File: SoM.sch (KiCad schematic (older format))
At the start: 6 parts, among them U8 SA800U-WF

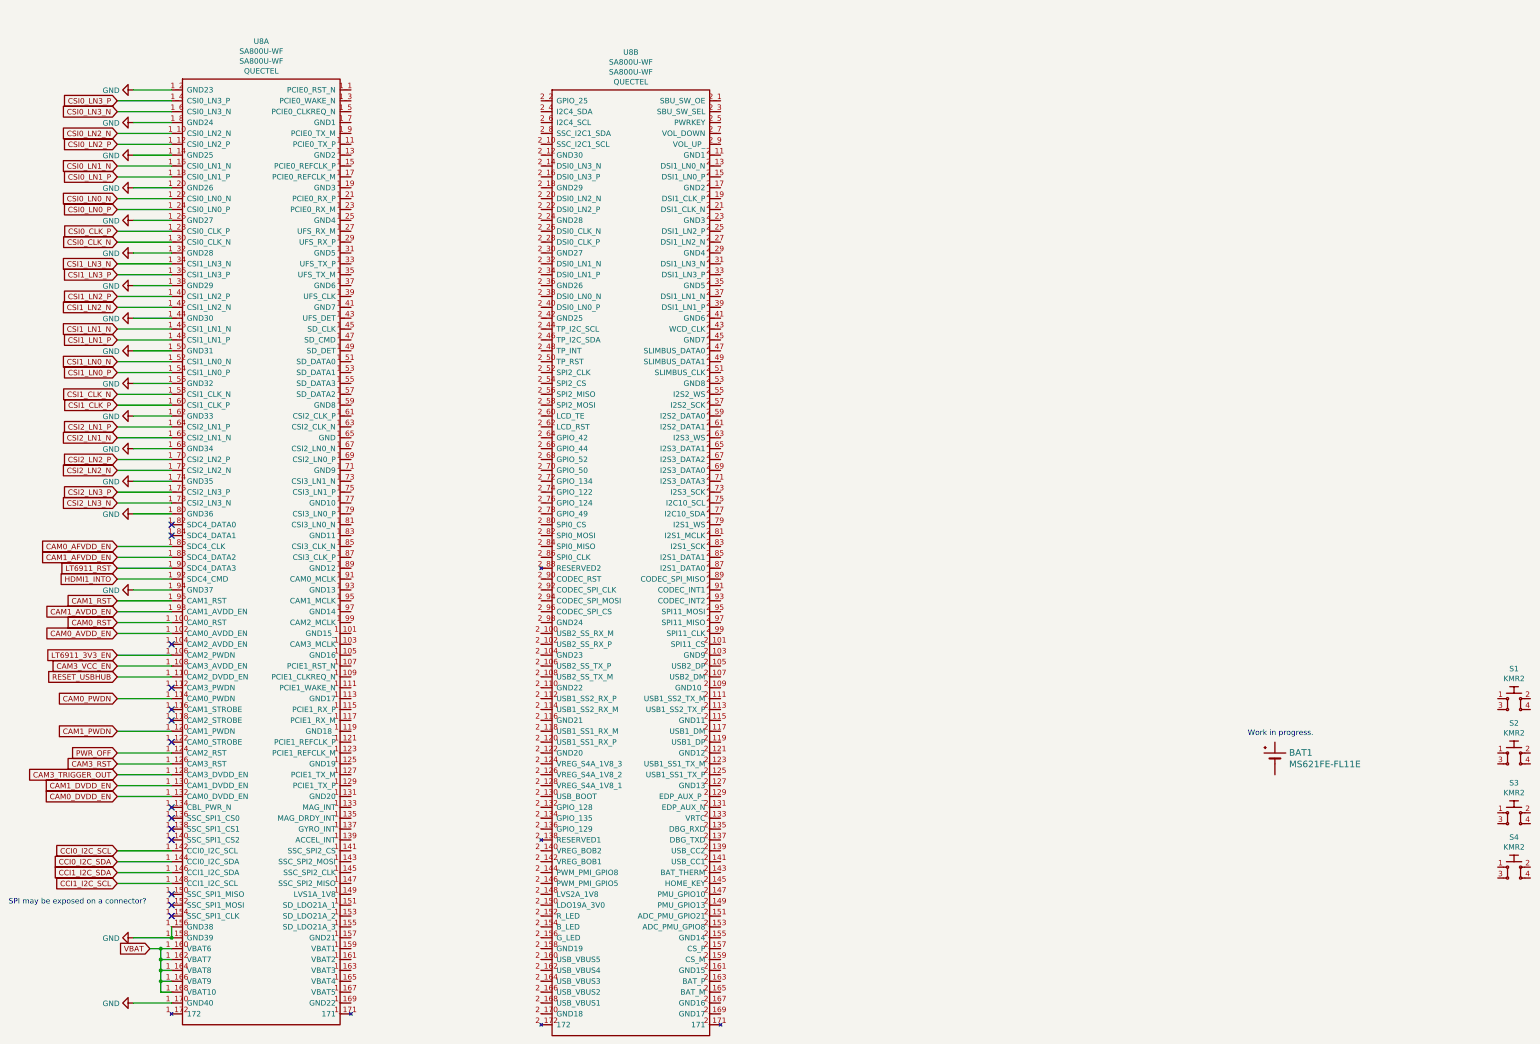
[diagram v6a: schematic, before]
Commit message: added an initial version of SoM
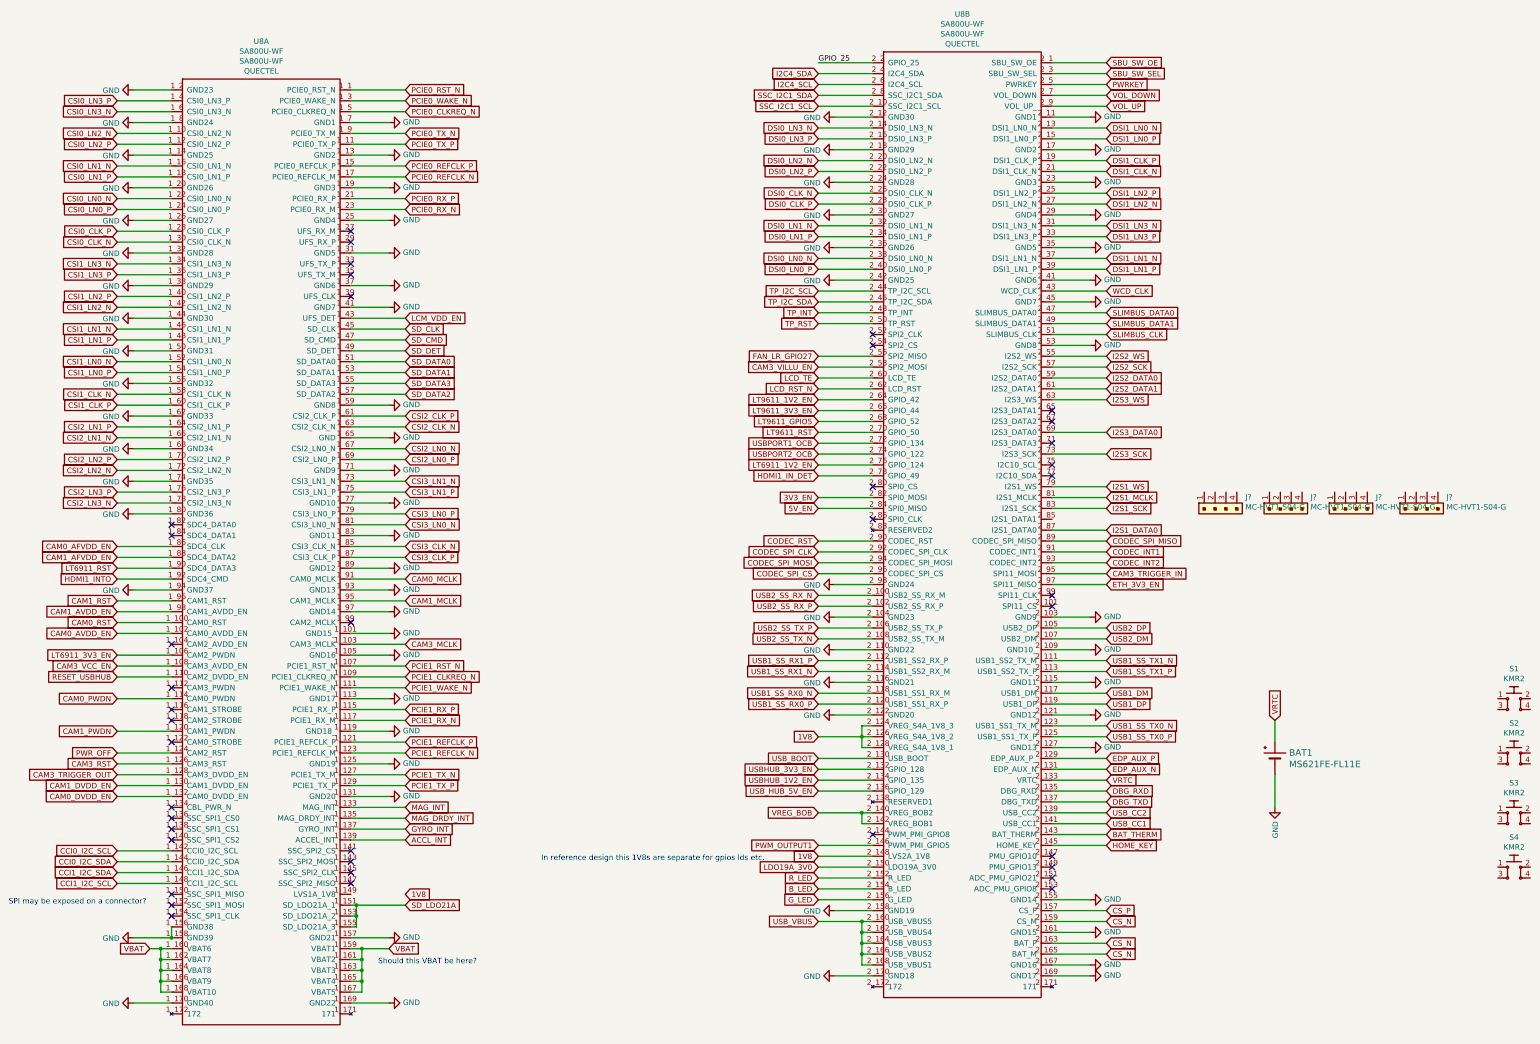
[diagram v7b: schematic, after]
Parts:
- added J? (x4): MC-HVT1-S04-G, antmicro-footprints:PinHeader_1x4_P1.27mm_Drill.7mm, symbol antmicroRectangularConnectorsHeadersMalePins:MC-HVT1-S04-G
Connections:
- net GND: now also BAT1.-, U8.1_101 (GND15_), U8.1_105 (GND16), U8.1_113 (GND17), U8.1_119 (GND18_), U8.1_125 (GND19), U8.1_13 (GND2), U8.1_131 (GND20), U8.1_157 (GND21), U8.1_169 (GND22), U8.1_19 (GND3), U8.1_25 (GND4), U8.1_31 (GND5), U8.1_37 (GND6), U8.1_41 (GND7), U8.1_59 (GND8), U8.1_65 (GND), U8.1_7 (GND1), U8.1_71 (GND9), U8.1_77 (GND10), U8.1_83 (GND11), U8.1_89 (GND12), U8.1_93 (GND13), U8.1_97 (GND14), U8.2_103 (GND9), U8.2_104 (GND23), U8.2_109 (GND10_), U8.2_11 (GND1), U8.2_110 (GND22), U8.2_115 (GND11), U8.2_116 (GND21), U8.2_12 (GND30), U8.2_121 (GND12), U8.2_122 (GND20), U8.2_127 (GND13), U8.2_155 (GND14), U8.2_158 (GND19), U8.2_161 (GND15), U8.2_167 (GND16), U8.2_169 (GND17), U8.2_17 (GND2), U8.2_170 (GND18), U8.2_18 (GND29), U8.2_23 (GND3), U8.2_24 (GND28), U8.2_29 (GND4), U8.2_30 (GND27), U8.2_35 (GND5), U8.2_36 (GND26), U8.2_41 (GND6), U8.2_42 (GND25), U8.2_45 (GND7), U8.2_53 (GND8), U8.2_98 (GND24)
- net VBAT: now also U8.1_159 (VBAT1), U8.1_161 (VBAT2), U8.1_163 (VBAT3), U8.1_165 (VBAT4), U8.1_167 (VBAT5)
- net VRTC: now reaches BAT1.+
- net VRTC: now also U8.2_133 (VRTC)
- net PCIE0_RST_N: now reaches U8.1_1 (PCIE0_RST_N)
- net CAM3_MCLK: now reaches U8.1_103 (CAM3_MCLK)
- net PCIE1_RST_N: now reaches U8.1_107 (PCIE1_RST_N)
- net PCIE1_CLKREQ_N: now reaches U8.1_109 (PCIE1_CLKREQ_N)
- net PCIE0_TX_P: now reaches U8.1_11 (PCIE0_TX_P)
- net PCIE1_WAKE_N: now reaches U8.1_111 (PCIE1_WAKE_N)
- net PCIE1_RX_P: now reaches U8.1_115 (PCIE1_RX_P)
- net PCIE1_RX_N: now reaches U8.1_117 (PCIE1_RX_M)
- net PCIE1_REFCLK_P: now reaches U8.1_121 (PCIE1_REFCLK_P)
- net PCIE1_REFCLK_N: now reaches U8.1_123 (PCIE1_REFCLK_M)
- net PCIE1_TX_N: now reaches U8.1_127 (PCIE1_TX_M)
- net PCIE1_TX_P: now reaches U8.1_129 (PCIE1_TX_P)
- net MAG_INT: now reaches U8.1_133 (MAG_INT)
- net MAG_DRDY_INT: now reaches U8.1_135 (MAG_DRDY_INT)
- net GYRO_INT: now reaches U8.1_137 (GYRO_INT)
- net ACCL_INT: now reaches U8.1_139 (ACCEL_INT)
- net PCIE0_REFCLK_P: now reaches U8.1_15 (PCIE0_REFCLK_P)
- net SD_LDO21A: now reaches U8.1_151 (SD_LDO21A_1)
- net SD_LDO21A: now also U8.1_153 (SD_LDO21A_2), U8.1_155 (SD_LDO21A_3)
- net PCIE0_REFCLK_N: now reaches U8.1_17 (PCIE0_REFCLK_M)
- net PCIE0_RX_P: now reaches U8.1_21 (PCIE0_RX_P)
- net PCIE0_RX_N: now reaches U8.1_23 (PCIE0_RX_M)
- net PCIE0_WAKE_N: now reaches U8.1_3 (PCIE0_WAKE_N)
- net LCM_VDD_EN: now reaches U8.1_43 (UFS_DET)
- net SD_CLK: now reaches U8.1_45 (SD_CLK)
- net SD_CMD: now reaches U8.1_47 (SD_CMD)
- net SD_DET: now reaches U8.1_49 (SD_DET)
- net PCIE0_CLKREQ_N: now reaches U8.1_5 (PCIE0_CLKREQ_N)
- net SD_DATA0: now reaches U8.1_51 (SD_DATA0)
- net SD_DATA1: now reaches U8.1_53 (SD_DATA1)
- net SD_DATA3: now reaches U8.1_55 (SD_DATA3)
- net SD_DATA2: now reaches U8.1_57 (SD_DATA2)
- net CSI2_CLK_P: now reaches U8.1_61 (CSI2_CLK_P)
- net CSI2_CLK_N: now reaches U8.1_63 (CSI2_CLK_N)
- net CSI2_LN0_N: now reaches U8.1_67 (CSI2_LN0_N)
- net CSI2_LN0_P: now reaches U8.1_69 (CSI2_LN0_P)
- net CSI3_LN1_N: now reaches U8.1_73 (CSI3_LN1_N)
- net CSI3_LN1_P: now reaches U8.1_75 (CSI3_LN1_P)
- net CSI3_LN0_P: now reaches U8.1_79 (CSI3_LN0_P)
- net CSI3_LN0_N: now reaches U8.1_81 (CSI3_LN0_N)
- net CSI3_CLK_N: now reaches U8.1_85 (CSI3_CLK_N)
- net CSI3_CLK_P: now reaches U8.1_87 (CSI3_CLK_P)
- net PCIE0_TX_N: now reaches U8.1_9 (PCIE0_TX_M)
- net CAM0_MCLK: now reaches U8.1_91 (CAM0_MCLK)
- net CAM1_MCLK: now reaches U8.1_95 (CAM1_MCLK)
- net SBU_SW_OE: now reaches U8.2_1 (SBU_SW_OE)
- net SSC_I2C1_SCL: now reaches U8.2_10 (SSC_I2C1_SCL)
- net USB2_SS_RX_N: now reaches U8.2_100 (USB2_SS_RX_M)
- net USB2_SS_RX_P: now reaches U8.2_102 (USB2_SS_RX_P)
- net USB2_DP: now reaches U8.2_105 (USB2_DP)
- net USB2_SS_TX_P: now reaches U8.2_106 (USB2_SS_TX_P)
- net USB2_DM: now reaches U8.2_107 (USB2_DM)
- net USB2_SS_TX_N: now reaches U8.2_108 (USB2_SS_TX_M)
- net USB1_SS_TX1_N: now reaches U8.2_111 (USB1_SS2_TX_M)
- net USB1_SS_RX1_P: now reaches U8.2_112 (USB1_SS2_RX_P)
- net USB1_SS_TX1_P: now reaches U8.2_113 (USB1_SS2_TX_P)
- net USB1_SS_RX1_N: now reaches U8.2_114 (USB1_SS2_RX_M)
- net USB1_DM: now reaches U8.2_117 (USB1_DM)
- net USB1_SS_RX0_N: now reaches U8.2_118 (USB1_SS1_RX_M)
- net USB1_DP: now reaches U8.2_119 (USB1_DP)
- net USB1_SS_RX0_P: now reaches U8.2_120 (USB1_SS1_RX_P)
- net USB1_SS_TX0_N: now reaches U8.2_123 (USB1_SS1_TX_M)
- net 1V8: now reaches U8.2_124 (VREG_S4A_1V8_3)
- net 1V8: now also U8.2_126 (VREG_S4A_1V8_2), U8.2_128 (VREG_S4A_1V8_1), U8.2_148 (LVS2A_1V8)
- net USB1_SS_TX0_P: now reaches U8.2_125 (USB1_SS1_TX_P)
- net EDP_AUX_P: now reaches U8.2_129 (EDP_AUX_P_)
- net DSI1_LN0_N: now reaches U8.2_13 (DSI1_LN0_N)
- net USB_BOOT: now reaches U8.2_130 (USB_BOOT)
- net EDP_AUX_N: now reaches U8.2_131 (EDP_AUX_N)
- net USBHUB_3V3_EN: now reaches U8.2_132 (GPIO_128)
- net USBHUB_1V2_EN: now reaches U8.2_134 (GPIO_135)
- net DBG_RXD: now reaches U8.2_135 (DBG_RXD)
- net USB_HUB_5V_EN: now reaches U8.2_136 (GPIO_129)
- net DBG_TXD: now reaches U8.2_137 (DBG_TXD)
- net USB_CC2: now reaches U8.2_139 (USB_CC2)
- net DSI0_LN3_N: now reaches U8.2_14 (DSI0_LN3_N)
- net VREG_BOB: now reaches U8.2_140 (VREG_BOB2)
- net VREG_BOB: now also U8.2_142 (VREG_BOB1)
- net USB_CC1: now reaches U8.2_141 (USB_CC1)
- net BAT_THERM: now reaches U8.2_143 (BAT_THERM)
- net HOME_KEY: now reaches U8.2_145 (HOME_KEY)
- net PWM_OUTPUT1: now reaches U8.2_146 (PWM_PMI_GPIO5)
- net DSI1_LN0_P: now reaches U8.2_15 (DSI1_LN0_P)
- net LDO19A_3V0: now reaches U8.2_150 (LDO19A_3V0)
- net R_LED: now reaches U8.2_152 (R_LED)
- net B_LED: now reaches U8.2_154 (B_LED)
- net G_LED: now reaches U8.2_156 (G_LED)
- net CS_P: now reaches U8.2_157 (CS_P)
- net CS_N: now reaches U8.2_159 (CS_M)
- net CS_N: now also U8.2_163 (BAT_P), U8.2_165 (BAT_M)
- net DSI0_LN3_P: now reaches U8.2_16 (DSI0_LN3_P)
- net USB_VBUS: now reaches U8.2_160 (USB_VBUS5)
- net USB_VBUS: now also U8.2_162 (USB_VBUS4), U8.2_164 (USB_VBUS3), U8.2_166 (USB_VBUS2), U8.2_168 (USB_VBUS1)
- net DSI1_CLK_P: now reaches U8.2_19 (DSI1_CLK_P)
- net GPIO_25: now reaches U8.2_2 (GPIO_25)
- net DSI0_LN2_N: now reaches U8.2_20 (DSI0_LN2_N)
- net DSI1_CLK_N: now reaches U8.2_21 (DSI1_CLK_N)
- net DSI0_LN2_P: now reaches U8.2_22 (DSI0_LN2_P)
- net DSI1_LN2_P: now reaches U8.2_25 (DSI1_LN2_P)
- net DSI0_CLK_N: now reaches U8.2_26 (DSI0_CLK_N)
- net DSI1_LN2_N: now reaches U8.2_27 (DSI1_LN2_N)
- net DSI0_CLK_P: now reaches U8.2_28 (DSI0_CLK_P)
- net SBU_SW_SEL: now reaches U8.2_3 (SBU_SW_SEL)
- net DSI1_LN3_N: now reaches U8.2_31 (DSI1_LN3_N)
- net DSI0_LN1_N: now reaches U8.2_32 (DSI0_LN1_N)
- net DSI1_LN3_P: now reaches U8.2_33 (DSI1_LN3_P)
- net DSI0_LN1_P: now reaches U8.2_34 (DSI0_LN1_P)
- net DSI1_LN1_N: now reaches U8.2_37 (DSI1_LN1_N)
- net DSI0_LN0_N: now reaches U8.2_38 (DSI0_LN0_N)
- net DSI1_LN1_P: now reaches U8.2_39 (DSI1_LN1_P)
- net I2C4_SDA: now reaches U8.2_4 (I2C4_SDA)
- net DSI0_LN0_P: now reaches U8.2_40 (DSI0_LN0_P)
- net WCD_CLK: now reaches U8.2_43 (WCD_CLK)
- net TP_I2C_SCL: now reaches U8.2_44 (TP_I2C_SCL)
- net TP_I2C_SDA: now reaches U8.2_46 (TP_I2C_SDA)
- net SLIMBUS_DATA0: now reaches U8.2_47 (SLIMBUS_DATA0)
- net TP_INT: now reaches U8.2_48 (TP_INT)
- net SLIMBUS_DATA1: now reaches U8.2_49 (SLIMBUS_DATA1)
- net PWRKEY: now reaches U8.2_5 (PWRKEY)
- net TP_RST: now reaches U8.2_50 (TP_RST)
- net SLIMBUS_CLK: now reaches U8.2_51 (SLIMBUS_CLK)
- net I2S2_WS: now reaches U8.2_55 (I2S2_WS)
- net FAN_LR_GPIO27: now reaches U8.2_56 (SPI2_MISO)
- net I2S2_SCK: now reaches U8.2_57 (I2S2_SCK)
- net CAM3_VILLU_EN: now reaches U8.2_58 (SPI2_MOSI)
- net I2S2_DATA0: now reaches U8.2_59 (I2S2_DATA0)
- net I2C4_SCL: now reaches U8.2_6 (I2C4_SCL)
- net LCD_TE: now reaches U8.2_60 (LCD_TE)
- net I2S2_DATA1: now reaches U8.2_61 (I2S2_DATA1)
- net LCD_RST_N: now reaches U8.2_62 (LCD_RST)
- net I2S3_WS: now reaches U8.2_63 (I2S3_WS)
- net LT9611_1V2_EN: now reaches U8.2_64 (GPIO_42)
- net LT9611_3V3_EN: now reaches U8.2_66 (GPIO_44)
- net LT9611_GPIO5: now reaches U8.2_68 (GPIO_52)
- net I2S3_DATA0: now reaches U8.2_69 (I2S3_DATA0)
- net VOL_DOWN: now reaches U8.2_7 (VOL_DOWN)
- net LT9611_RST: now reaches U8.2_70 (GPIO_50)
- net USBPORT1_OCB: now reaches U8.2_72 (GPIO_134)
- net I2S3_SCK: now reaches U8.2_73 (I2S3_SCK)
- net USBPORT2_OCB: now reaches U8.2_74 (GPIO_122)
- net LT6911_1V2_EN: now reaches U8.2_76 (GPIO_124)
- net HDMI1_IN_DET: now reaches U8.2_78 (GPIO_49)
- net I2S1_WS: now reaches U8.2_79 (I2S1_WS)
- net SSC_I2C1_SDA: now reaches U8.2_8 (SSC_I2C1_SDA)
- net I2S1_MCLK: now reaches U8.2_81 (I2S1_MCLK)
- net 3V3_EN: now reaches U8.2_82 (SPI0_MOSI)
- net I2S1_SCK: now reaches U8.2_83 (I2S1_SCK)
- net 5V_EN: now reaches U8.2_84 (SPI0_MISO)
- net I2S1_DATA0: now reaches U8.2_87 (I2S1_DATA0)
- net CODEC_SPI_MISO: now reaches U8.2_89 (CODEC_SPI_MISO)
- net VOL_UP: now reaches U8.2_9 (VOL_UP_)
- net CODEC_RST: now reaches U8.2_90 (CODEC_RST)
- net CODEC_INT1: now reaches U8.2_91 (CODEC_INT1)
- net CODEC_SPI_CLK: now reaches U8.2_92 (CODEC_SPI_CLK)
- net CODEC_INT2: now reaches U8.2_93 (CODEC_INT2)
- net CODEC_SPI_MOSI: now reaches U8.2_94 (CODEC_SPI_MOSI)
- net CAM3_TRIGGER_IN: now reaches U8.2_95 (SPI11_MOSI)
- net CODEC_SPI_CS: now reaches U8.2_96 (CODEC_SPI_CS)
- net ETH_3V3_EN: now reaches U8.2_97 (SPI11_MISO)
- no-connect marks 14 -> 40
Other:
- note added: "In reference design this 1V8s are separate for gpios lds etc.\n"
- note added: "Should this VBAT be here?\n"
- note removed: "Work in progress."
- moved on the sheet: U8B

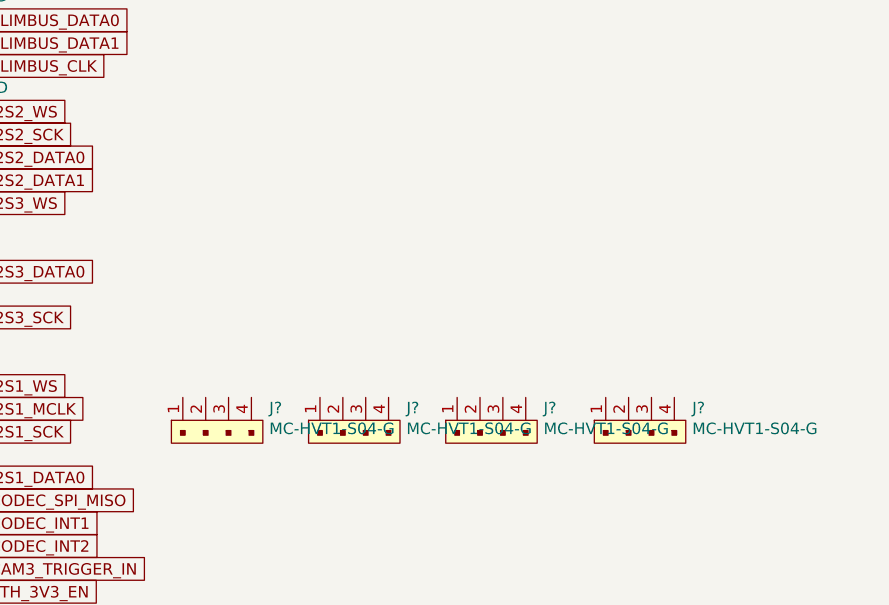
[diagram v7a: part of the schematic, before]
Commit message: re-evaluated gpios
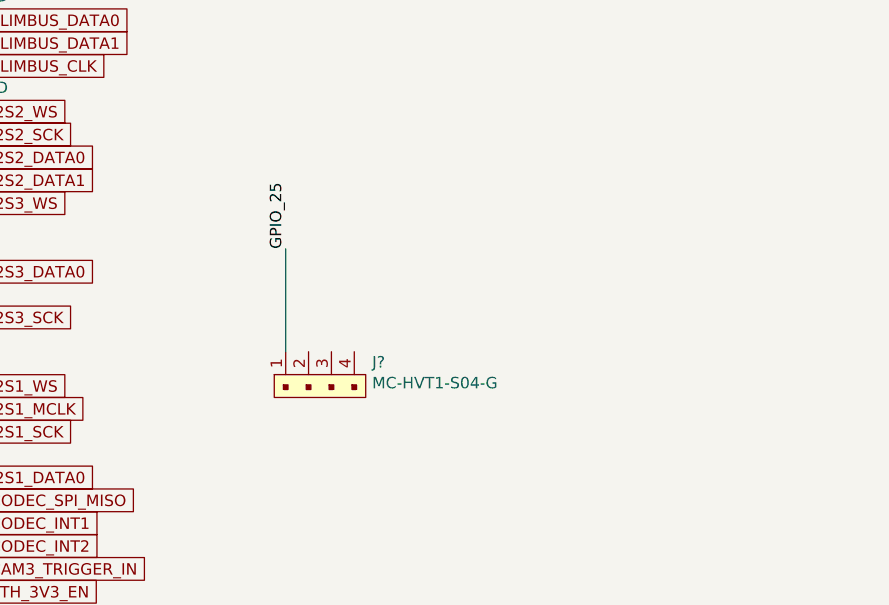
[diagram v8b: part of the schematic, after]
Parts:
- removed J? (x3): MC-HVT1-S04-G, antmicro-footprints:PinHeader_1x4_P1.27mm_Drill.7mm, symbol antmicroRectangularConnectorsHeadersMalePins:MC-HVT1-S04-G
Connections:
- net GPIO_25: now also J?.1
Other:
- moved on the sheet: J?
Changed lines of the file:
@@
 L antmicroRectangularConnectorsHeadersMalePins:MC-HVT1-S04-G J?
 U 1 1 61E93EA5
-P 11150 5600
-F 0 "J?" H 11528 5704 50  0000 L CNN
-F 1 "MC-HVT1-S04-G" H 11528 5613 50  0000 L CNN
-F 2 "antmicro-footprints:PinHeader_1x4_P1.27mm_Drill.7mm" H 11350 5900 60  0001 L CNN
-F 3 "http://www.farnell.com/datasheets/2605295.pdf" H 11350 6000 60  0001 L CNN
-F 4 "MC-HVT1-S04-G" H 11350 6100 60  0001 L CNN "MPN"
-F 5 "Multicomp" H 11350 6200 60  0001 L CNN "Manufacturer"
-	1    11150 5600
-	1    0    0    -1
-$EndComp
-$Comp
-L antmicroRectangularConnectorsHeadersMalePins:MC-HVT1-S04-G J?
-U 1 1 61E93EAD
-P 11750 5600
-F 0 "J?" H 12128 5704 50  0000 L CNN
-F 1 "MC-HVT1-S04-G" H 12128 5613 50  0000 L CNN
-F 2 "antmicro-footprints:PinHeader_1x4_P1.27mm_Drill.7mm" H 11950 5900 60  0001 L CNN
-F 3 "http://www.farnell.com/datasheets/2605295.pdf" H 11950 6000 60  0001 L CNN
-F 4 "MC-HVT1-S04-G" H 11950 6100 60  0001 L CNN "MPN"
-F 5 "Multicomp" H 11950 6200 60  0001 L CNN "Manufacturer"
-	1    11750 5600
-	1    0    0    -1
-$EndComp
-$Comp
-L antmicroRectangularConnectorsHeadersMalePins:MC-HVT1-S04-G J?
-U 1 1 61E93EB5
-P 12350 5600
-F 0 "J?" H 12728 5704 50  0000 L CNN
-F 1 "MC-HVT1-S04-G" H 12728 5613 50  0000 L CNN
-F 2 "antmicro-footprints:PinHeader_1x4_P1.27mm_Drill.7mm" H 12550 5900 60  0001 L CNN
-F 3 "http://www.farnell.com/datasheets/2605295.pdf" H 12550 6000 60  0001 L CNN
-F 4 "MC-HVT1-S04-G" H 12550 6100 60  0001 L CNN "MPN"
-F 5 "Multicomp" H 12550 6200 60  0001 L CNN "Manufacturer"
-	1    12350 5600
-	1    0    0    -1
-$EndComp
-$Comp
-L antmicroRectangularConnectorsHeadersMalePins:MC-HVT1-S04-G J?
-U 1 1 61E93EBD
-P 13000 5600
-F 0 "J?" H 13378 5704 50  0000 L CNN
-F 1 "MC-HVT1-S04-G" H 13378 5613 50  0000 L CNN
-F 2 "antmicro-footprints:PinHeader_1x4_P1.27mm_Drill.7mm" H 13200 5900 60  0001 L CNN
-F 3 "http://www.farnell.com/datasheets/2605295.pdf" H 13200 6000 60  0001 L CNN
-F 4 "MC-HVT1-S04-G" H 13200 6100 60  0001 L CNN "MPN"
-F 5 "Multicomp" H 13200 6200 60  0001 L CNN "Manufacturer"
-	1    13000 5600
+P 11600 5400
+F 0 "J?" H 11978 5504 50  0000 L CNN
+F 1 "MC-HVT1-S04-G" H 11978 5413 50  0000 L CNN
+F 2 "antmicro-footprints:PinHeader_1x4_P1.27mm_Drill.7mm" H 11800 5700 60  0001 L CNN
+F 3 "http://www.farnell.com/datasheets/2605295.pdf" H 11800 5800 60  0001 L CNN
+F 4 "MC-HVT1-S04-G" H 11800 5900 60  0001 L CNN "MPN"
+F 5 "Multicomp" H 11800 6000 60  0001 L CNN "Manufacturer"
+	1    11600 5400
 	1    0    0    -1
 $EndComp
@@
 Wire Wire Line
 	11800 8050 11800 8350
+Wire Wire Line
+	11600 5250 11600 4800
+Text Label 11600 4800 1    50   ~ 0
+GPIO_25
 $EndSCHEMATC
